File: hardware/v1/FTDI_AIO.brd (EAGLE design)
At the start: 49.5 x 49.5 mm, 45 parts, among them IC1 MCP1702-3.3, IC2 FT232RL, X1 ISP, X2 USB-A-H, X3 UART

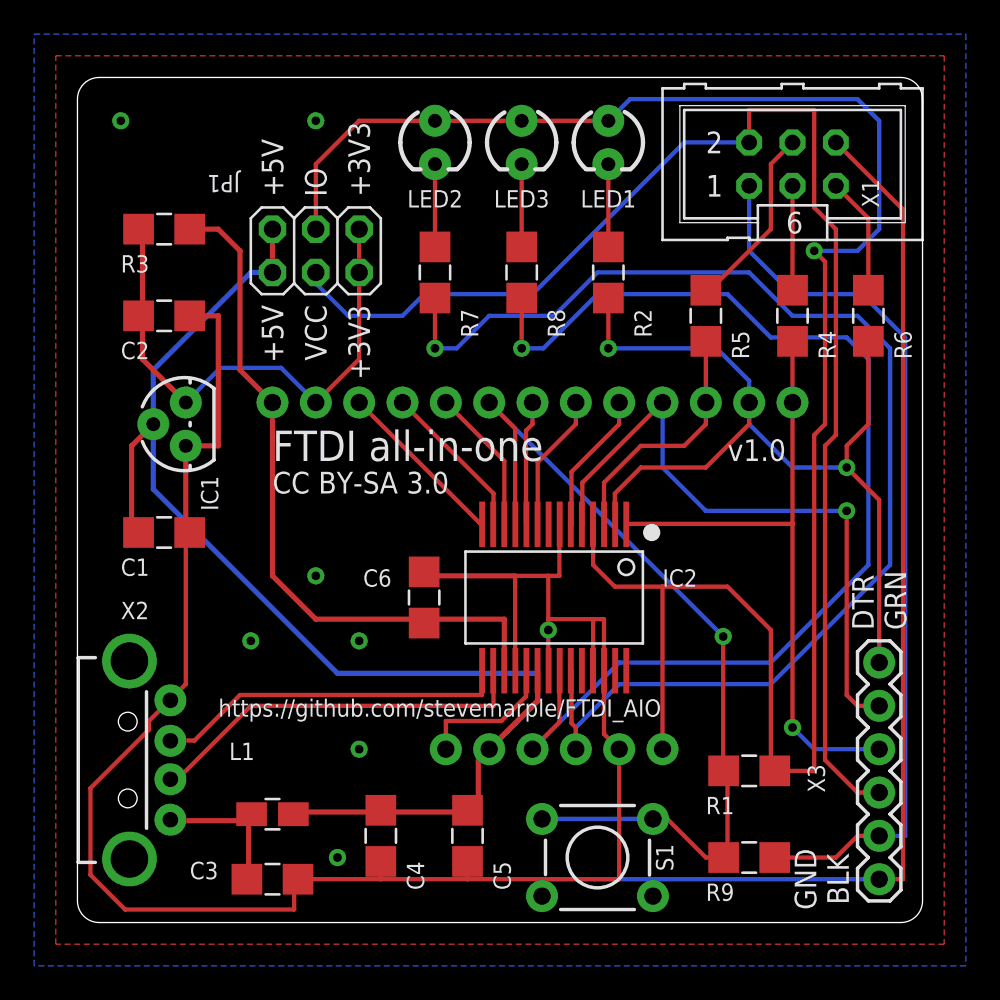
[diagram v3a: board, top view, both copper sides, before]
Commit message: Adding decoupling capacitor for FT232R VCCIO.
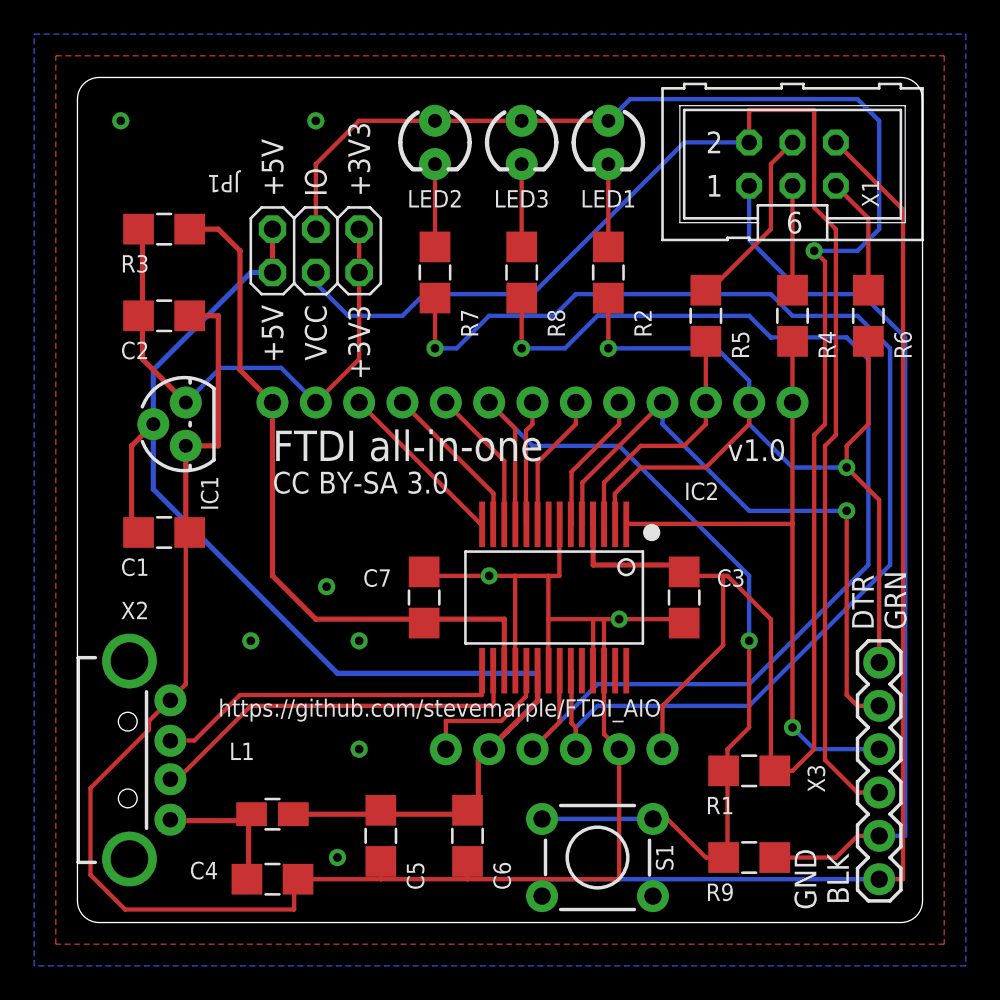
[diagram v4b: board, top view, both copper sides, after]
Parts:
- added C7: 100n, SteveMarple:1206-HAND
- C3: value 10n -> 100n
- C4: value 4u7 -> 10n
- C5: value 100n -> 4u7
- moved C3 29.2 mm to (35.6, 19.1), turned to 270 degrees
- moved C6 14.2 mm to (22.9, 5.08), turned to 270 degrees
- moved U$13 7.62 mm to (29.2, 10.2)
- moved U$14 7.62 mm to (21.6, 10.2)
- moved C4 6.84 mm to (11.4, 2.54), turned to 0 degrees
- moved C5 5.08 mm to (17.8, 5.08)
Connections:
- net !RESET: now also U$14.1; no longer U$13.1
- net 3V3_OUT: now also C7.1; no longer C6.1
- net GND: now also C7.2
- net TXLED: now also U$13.1; no longer U$14.1
- net VBUS_FILT: now also C6.1; no longer C4.1
- net VCC: now also C3.1
- net VUSB: now also C4.1; no longer C3.1
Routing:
- net GND: track 188.3 -> 193.3 mm, vias 8 -> 9
- net CTS: track 52.2 -> 56.3 mm
- net VCC: track 115.3 -> 118.1 mm
- net RX: track 37.7 -> 36.2 mm
- net TXLED: track 74.6 -> 73.5 mm
- net RXLED: track 67.6 -> 66.6 mm

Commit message: Ensuring all silkscreen is within board outline.
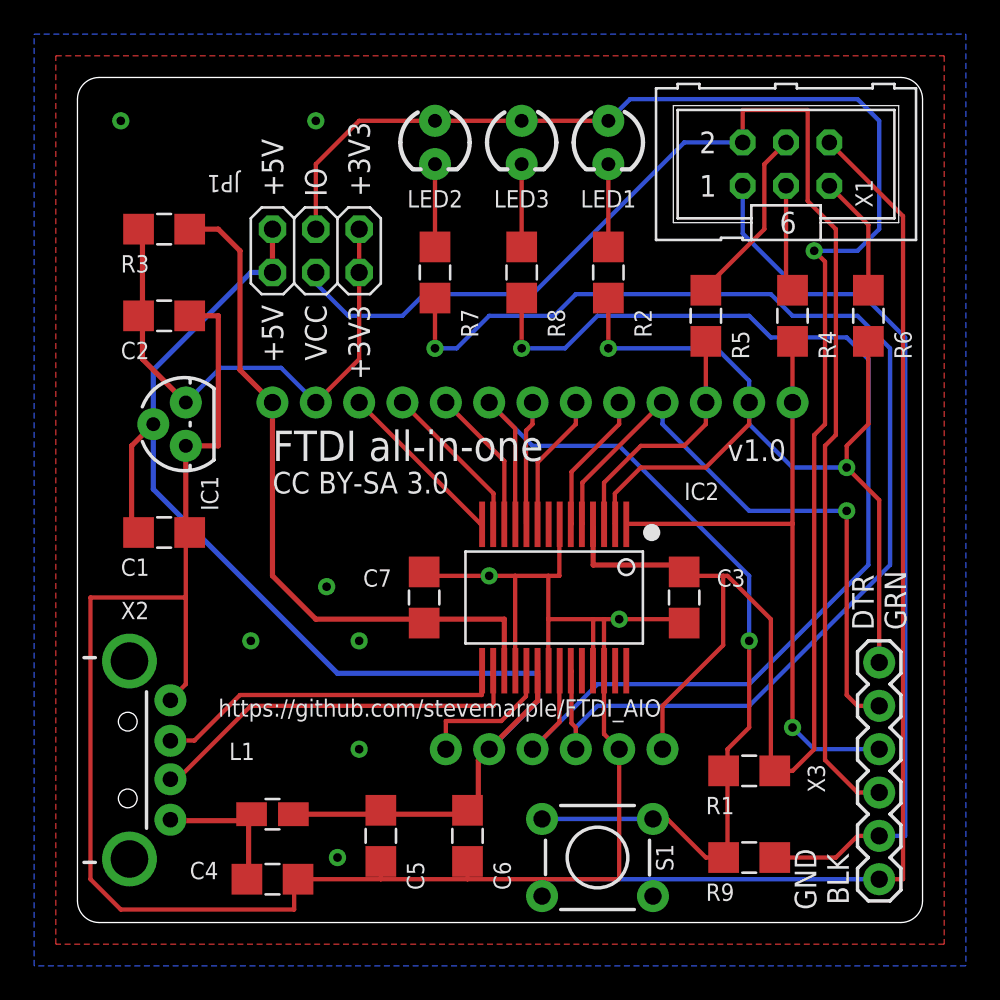
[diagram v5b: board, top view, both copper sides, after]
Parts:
- X2: device SparkFun:USB-A-H -> SteveMarple:USB-A-H
- moved X1 0.38 mm to (41.5, 44.5)
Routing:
- net GND: track 193.3 -> 203.3 mm
- net N$2: track 11.2 -> 10.6 mm
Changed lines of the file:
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@@
 <attribute name="VALUE" x="9.525" y="45.085" size="1.016" layer="27" ratio="10" rot="SR180"/>
 </element>
-<element name="X1" library="SteveMarple" package="CONN-HARTING-ML6" value="ISP" x="41.91" y="44.45" smashed="yes">
-<attribute name="NAME" x="46.99" y="41.91" size="1.016" layer="25" ratio="10" rot="R90"/>
-<attribute name="VALUE" x="46.99" y="45.085" size="1.016" layer="27" ratio="10" rot="R90"/>
+<element name="X1" library="SteveMarple" package="CONN-HARTING-ML6" value="ISP" x="41.529" y="44.45" smashed="yes">
+<attribute name="NAME" x="46.609" y="41.91" size="1.016" layer="25" ratio="10" rot="R90"/>
+<attribute name="VALUE" x="46.609" y="45.085" size="1.016" layer="27" ratio="10" rot="R90"/>
 </element>
 <element name="LED1" library="SparkFun" package="LED3MM" value="AUX" x="31.115" y="45.72" smashed="yes" rot="R270">
@@
 <attribute name="VALUE" x="33.655" y="37.465" size="1.016" layer="27" ratio="10" rot="R90"/>
 </element>
-<element name="X2" library="SparkFun" package="USB-A-H" value="USB-A-H" x="3.048" y="9.525" smashed="yes">
+<element name="X2" library="SteveMarple" package="USB-A-H" value="USB-A-H" x="3.048" y="9.525" smashed="yes">
 <attribute name="NAME" x="2.54" y="17.78" size="1.016" layer="25" ratio="10"/>
 </element>
@@
 <contactref element="C2" pad="2"/>
 <contactref element="C1" pad="2"/>
-<wire x1="48.387" y1="41.783" x2="44.45" y2="45.72" width="0.254" layer="1"/>
-<wire x1="48.387" y1="2.54" x2="48.387" y2="41.783" width="0.254" layer="1"/>
+<wire x1="48.387" y1="41.402" x2="44.069" y2="45.72" width="0.254" layer="1"/>
+<wire x1="48.387" y1="2.54" x2="48.387" y2="41.402" width="0.254" layer="1"/>
 <wire x1="46.99" y1="2.54" x2="48.387" y2="2.54" width="0.254" layer="1"/>
 <wire x1="6.477" y1="35.56" x2="6.579" y2="35.56" width="0.254" layer="1"/>
@@
 <wire x1="30.226" y1="17.78" x2="27.5971" y2="17.78" width="0.254" layer="1"/>
 <wire x1="30.226" y1="14.859" x2="30.226" y2="17.78" width="0.254" layer="1"/>
-<wire x1="4.191" y1="11.811" x2="5.334" y2="12.954" width="0.254" layer="1"/>
-<wire x1="4.191" y1="11.303" x2="4.191" y2="11.811" width="0.254" layer="1"/>
-<wire x1="0.762" y1="7.874" x2="4.191" y2="11.303" width="0.254" layer="1"/>
-<wire x1="0.762" y1="2.794" x2="0.762" y2="7.874" width="0.254" layer="1"/>
-<wire x1="2.794" y1="0.762" x2="0.762" y2="2.794" width="0.254" layer="1"/>
-<wire x1="12.7" y1="0.762" x2="2.794" y2="0.762" width="0.254" layer="1"/>
+<wire x1="0.762" y1="19.05" x2="6.35" y2="19.05" width="0.254" layer="1"/>
+<wire x1="0.762" y1="2.54" x2="0.762" y2="19.05" width="0.254" layer="1"/>
+<wire x1="2.54" y1="0.762" x2="0.762" y2="2.54" width="0.254" layer="1"/>
+<wire x1="12.7" y1="0.762" x2="2.54" y2="0.762" width="0.254" layer="1"/>
 <wire x1="12.7" y1="2.54" x2="12.7" y2="0.762" width="0.254" layer="1"/>
-<wire x1="5.334" y1="12.954" x2="5.448" y2="13.025" width="0.254" layer="1"/>
 <wire x1="27.2288" y1="2.54" x2="22.86" y2="2.54" width="0.254" layer="1"/>
 <wire x1="22.86" y1="2.54" x2="17.78" y2="2.54" width="0.254" layer="1"/>
@@
 <wire x1="8.255" y1="27.94" x2="8.255" y2="35.56" width="0.3048" layer="1"/>
 <wire x1="6.35" y1="27.94" x2="8.255" y2="27.94" width="0.3048" layer="1"/>
-<wire x1="6.35" y1="13.97" x2="6.35" y2="22.86" width="0.254" layer="1"/>
+<wire x1="6.35" y1="13.97" x2="6.35" y2="19.05" width="0.254" layer="1"/>
+<wire x1="6.35" y1="19.05" x2="6.35" y2="22.86" width="0.254" layer="1"/>
 <wire x1="5.461" y1="13.081" x2="6.35" y2="13.97" width="0.254" layer="1"/>
 <wire x1="6.35" y1="22.86" x2="6.579" y2="22.86" width="0.254" layer="1"/>
@@
 <contactref element="X1" pad="2"/>
 <wire x1="26.67" y1="36.83" x2="35.56" y2="45.72" width="0.254" layer="16"/>
-<wire x1="35.56" y1="45.72" x2="39.37" y2="45.72" width="0.254" layer="16"/>
+<wire x1="35.56" y1="45.72" x2="38.989" y2="45.72" width="0.254" layer="16"/>
 <wire x1="15.875" y1="35.56" x2="19.05" y2="35.56" width="0.254" layer="16"/>
 <wire x1="19.05" y1="35.56" x2="20.32" y2="36.83" width="0.254" layer="16"/>
@@
 <wire x1="43.815" y1="27.94" x2="43.815" y2="9.525" width="0.254" layer="1"/>
 <wire x1="43.815" y1="9.525" x2="45.72" y2="7.62" width="0.254" layer="1"/>
-<wire x1="43.18" y1="41.91" x2="44.45" y2="40.64" width="0.254" layer="1"/>
-<wire x1="43.18" y1="47.625" x2="43.18" y2="41.91" width="0.254" layer="1"/>
-<wire x1="39.37" y1="47.625" x2="43.18" y2="47.625" width="0.254" layer="1"/>
-<wire x1="39.37" y1="45.72" x2="39.37" y2="47.625" width="0.254" layer="1"/>
+<wire x1="42.799" y1="42.291" x2="44.45" y2="40.64" width="0.254" layer="1"/>
+<wire x1="42.799" y1="47.625" x2="42.799" y2="42.291" width="0.254" layer="1"/>
+<wire x1="38.989" y1="47.625" x2="42.799" y2="47.625" width="0.254" layer="1"/>
+<wire x1="38.989" y1="45.72" x2="38.989" y2="47.625" width="0.254" layer="1"/>
 </signal>
 <signal name="3V3_OUT">
@@
 <wire x1="48.514" y1="34.29" x2="45.974" y2="36.83" width="0.254" layer="16"/>
 <wire x1="45.974" y1="36.83" x2="42.545" y2="36.83" width="0.254" layer="16"/>
-<wire x1="42.545" y1="36.83" x2="39.37" y2="40.005" width="0.254" layer="16"/>
-<wire x1="39.37" y1="40.005" x2="39.37" y2="43.18" width="0.254" layer="16"/>
+<wire x1="42.545" y1="36.83" x2="38.989" y2="40.386" width="0.254" layer="16"/>
+<wire x1="38.989" y1="40.386" x2="38.989" y2="43.18" width="0.254" layer="16"/>
 <wire x1="48.514" y1="5.08" x2="48.514" y2="34.29" width="0.254" layer="16"/>
 <wire x1="46.99" y1="5.08" x2="48.514" y2="5.08" width="0.254" layer="16"/>
@@
 <contactref element="X1" pad="4"/>
 <contactref element="R5" pad="1"/>
-<wire x1="40.64" y1="40.64" x2="36.83" y2="36.83" width="0.254" layer="1"/>
-<wire x1="40.64" y1="44.45" x2="40.64" y2="40.64" width="0.254" layer="1"/>
-<wire x1="41.91" y1="45.72" x2="40.64" y2="44.45" width="0.254" layer="1"/>
-<wire x1="36.83" y1="36.83" x2="36.83" y2="37.059" width="0.254" layer="1"/>
+<wire x1="40.259" y1="40.64" x2="36.83" y2="37.211" width="0.254" layer="1"/>
+<wire x1="40.259" y1="44.45" x2="40.259" y2="40.64" width="0.254" layer="1"/>
+<wire x1="41.529" y1="45.72" x2="40.259" y2="44.45" width="0.254" layer="1"/>
+<wire x1="36.83" y1="37.211" x2="36.83" y2="37.059" width="0.254" layer="1"/>
 </signal>
 <signal name="SCK">
 <contactref element="X1" pad="3"/>
 <contactref element="R4" pad="2"/>
-<wire x1="41.91" y1="43.18" x2="41.91" y2="37.059" width="0.254" layer="1"/>
+<wire x1="41.529" y1="43.18" x2="41.529" y2="37.465" width="0.254" layer="1"/>
+<wire x1="41.529" y1="37.465" x2="41.91" y2="37.465" width="0.254" layer="1"/>
+<wire x1="41.91" y1="37.465" x2="41.91" y2="37.059" width="0.254" layer="1"/>
 </signal>
 <signal name="RST">
 <contactref element="X1" pad="5"/>
 <contactref element="R6" pad="2"/>
-<wire x1="46.355" y1="41.275" x2="46.355" y2="37.059" width="0.254" layer="1"/>
-<wire x1="44.45" y1="43.18" x2="46.355" y2="41.275" width="0.254" layer="1"/>
+<wire x1="46.355" y1="40.894" x2="46.355" y2="37.059" width="0.254" layer="1"/>
+<wire x1="44.069" y1="43.18" x2="46.355" y2="40.894" width="0.254" layer="1"/>
 </signal>
 <signal name="!RESET">
